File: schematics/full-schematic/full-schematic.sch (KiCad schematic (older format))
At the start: 24 parts, among them SW1 SW_SPST, SW2 SW_Push_Dual, SW3 SW_Push_Dual, SW4 SW_SPDT, U1 L7805, U2 74LS04, U5 LP3470, X1 CXO_DIP8

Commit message: Schematics
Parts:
- added TP2, TP3: TestPoint_Probe, TestPoint:TestPoint_Pad_D1.5mm, symbol Connector:TestPoint_Probe
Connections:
- net -RST-: now also TP2.1
- net SYS_CLK: now also TP3.1
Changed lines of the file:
@@
 EESchema Schematic File Version 4
-LIBS:full-schematic-cache
-EELAYER 29 0
+EELAYER 30 0
 EELAYER END
 $Descr A4 11693 8268
 encoding utf-8
-Sheet 1 3
+Sheet 1 4
 Title ""
 Date ""
@@
 	3400 5600 4050 5600
 Wire Wire Line
-	4550 6100 5000 6100
-Text Label 5000 6100 2    50   ~ 0
-SYS_CLK
+	4550 6100 4800 6100
 $Comp
 L power:VDD #PWR0101
@@
 	1    0    0    -1
 $EndComp
-$Comp
-L power:GND #PWR010
-U 1 1 5D4C31C1
-P 3900 4150
-F 0 "#PWR010" H 3900 3900 50  0001 C CNN
-F 1 "GND" H 3905 3977 50  0000 C CNN
-F 2 "" H 3900 4150 50  0001 C CNN
-F 3 "" H 3900 4150 50  0001 C CNN
-	1    3900 4150
-	1    0    0    -1
-$EndComp
-Wire Wire Line
-	3750 3700 3900 3700
-Connection ~ 3900 3700
-Wire Wire Line
-	3900 3850 3900 3700
 Wire Wire Line
 	3350 3700 3450 3700
 Wire Wire Line
 	3350 3550 3350 3700
-$Comp
-L Device:C C6
-U 1 1 5D4B9F93
-P 3900 4000
-F 0 "C6" H 4015 4046 50  0000 L CNN
-F 1 "0.1u" H 4015 3955 50  0000 L CNN
-F 2 "Capacitor_SMD:C_0603_1608Metric_Pad1.05x0.95mm_HandSolder" H 3938 3850 50  0001 C CNN
-F 3 "~" H 3900 4000 50  0001 C CNN
-	1    3900 4000
-	1    0    0    -1
-$EndComp
 $Comp
 L Device:R R5
@@
 $EndSheet
 Wire Wire Line
-	4050 3700 3900 3700
-Text Label 5650 4100 2    50   ~ 0
--RST-
-Wire Wire Line
-	5350 4100 5650 4100
-Wire Wire Line
-	4700 3700 5650 3700
-Connection ~ 4700 3700
-Wire Wire Line
-	4700 4100 4750 4100
-Wire Wire Line
-	4700 3700 4700 4100
+	5350 4100 5450 4100
+$Comp
+L z80-project:LP3470 U5
+U 1 1 5DDDF23A
+P 2100 3350
+F 0 "U5" H 1800 3650 50  0000 L CNN
+F 1 "LP3470" H 2200 3650 50  0000 L CNN
+F 2 "Package_TO_SOT_SMD:SOT-23-5_HandSoldering" H 3100 3000 50  0001 C CNN
+F 3 "https://www.promelec.ru/pdf/LP3470.pdf" H 3100 3000 50  0001 C CNN
+	1    2100 3350
+	1    0    0    -1
+$EndComp
+$Comp
+L power:GND #PWR017
+U 1 1 5DE0F4DA
+P 2100 4400
+F 0 "#PWR017" H 2100 4150 50  0001 C CNN
+F 1 "GND" H 2105 4227 50  0000 C CNN
+F 2 "" H 2100 4400 50  0001 C CNN
+F 3 "" H 2100 4400 50  0001 C CNN
+	1    2100 4400
+	1    0    0    -1
+$EndComp
+$Comp
+L power:+5V #PWR06
+U 1 1 5DE116D4
+P 2100 2850
+F 0 "#PWR06" H 2100 2700 50  0001 C CNN
+F 1 "+5V" H 2115 3023 50  0000 C CNN
+F 2 "" H 2100 2850 50  0001 C CNN
+F 3 "" H 2100 2850 50  0001 C CNN
+	1    2100 2850
+	1    0    0    -1
+$EndComp
+Wire Wire Line
+	1550 3200 1600 3200
+$Comp
+L Device:C C9
+U 1 1 5DE1D4C5
+P 1450 3700
+F 0 "C9" H 1565 3746 50  0000 L CNN
+F 1 "0.1u" H 1565 3655 50  0000 L CNN
+F 2 "Capacitor_SMD:C_0603_1608Metric_Pad1.05x0.95mm_HandSolder" H 1488 3550 50  0001 C CNN
+F 3 "~" H 1450 3700 50  0001 C CNN
+	1    1450 3700
+	1    0    0    -1
+$EndComp
+$Comp
+L power:GND #PWR05
+U 1 1 5DE1D99B
+P 1450 3850
+F 0 "#PWR05" H 1450 3600 50  0001 C CNN
+F 1 "GND" H 1455 3677 50  0000 C CNN
+F 2 "" H 1450 3850 50  0001 C CNN
+F 3 "" H 1450 3850 50  0001 C CNN
+	1    1450 3850
+	1    0    0    -1
+$EndComp
+Wire Wire Line
+	2100 2900 2100 3000
+Wire Wire Line
+	1550 2900 1550 3200
+Connection ~ 2100 2900
+Wire Wire Line
+	2100 2900 1550 2900
+Wire Wire Line
+	2100 2850 2100 2900
+Wire Wire Line
+	1450 3550 1450 3500
+Wire Wire Line
+	1450 3500 1600 3500
+$Sheet
+S 9500 1000 1500 500
+U 5DEAD379
+F0 "IC-Power" 50
+F1 "IC-Power.sch" 50
+$EndSheet
+Wire Wire Line
+	2650 3950 2700 3950
+Wire Wire Line
+	2700 4150 2650 4150
+Wire Wire Line
+	2100 3700 2100 3950
+Wire Wire Line
+	2250 3950 2100 3950
+Connection ~ 2100 3950
+Wire Wire Line
+	2100 3950 2100 4150
+Wire Wire Line
+	2250 4150 2100 4150
+Connection ~ 2100 4150
+Wire Wire Line
+	2100 4150 2100 4400
+$Comp
+L Device:D_Schottky D3
+U 1 1 5E366A87
+P 2900 3350
+F 0 "D3" H 2900 3250 50  0000 C CNN
+F 1 "D_Schottky" H 2900 3450 50  0000 C CNN
+F 2 "Diode_SMD:D_0603_1608Metric_Pad1.05x0.95mm_HandSolder" H 2900 3350 50  0001 C CNN
+F 3 "~" H 2900 3350 50  0001 C CNN
+	1    2900 3350
+	1    0    0    -1
+$EndComp
+Wire Wire Line
+	2750 3350 2600 3350
+Wire Wire Line
+	2700 3950 2700 4050
+Connection ~ 2700 4050
+Wire Wire Line
+	2700 4050 2700 4150
+Wire Wire Line
+	3050 3350 3200 3350
+Wire Wire Line
+	3200 3350 3200 3700
+Connection ~ 3200 3700
+Wire Wire Line
+	3200 3700 3200 4050
+Wire Wire Line
+	3200 3700 3350 3700
+Connection ~ 3350 3700
+Wire Wire Line
+	2700 4050 3200 4050
+Wire Wire Line
+	4650 3700 4700 3700
+$Comp
+L 74xx:74LS04 U2
+U 1 1 5D5B39DE
+P 4350 3700
+F 0 "U2" H 4350 4017 50  0000 C CNN
+F 1 "74LS04" H 4350 3926 50  0000 C CNN
+F 2 "Package_SO:SOIC-14_3.9x8.7mm_P1.27mm" H 4350 3700 50  0001 C CNN
+F 3 "http://www.ti.com/lit/gpn/sn74LS04" H 4350 3700 50  0001 C CNN
+	1    4350 3700
+	1    0    0    -1
+$EndComp
 $Comp
 L 74xx:74LS04 U2
@@
 	1    0    0    -1
 $EndComp
-Text Label 5650 3700 2    50   ~ 0
+Wire Wire Line
+	4700 3700 4700 4100
+Wire Wire Line
+	4700 4100 4750 4100
+Connection ~ 4700 3700
+Wire Wire Line
+	4700 3700 5650 3700
+Wire Wire Line
+	4050 3700 3900 3700
+$Comp
+L Device:C C6
+U 1 1 5D4B9F93
+P 3900 4000
+F 0 "C6" H 4015 4046 50  0000 L CNN
+F 1 "0.1u" H 4015 3955 50  0000 L CNN
+F 2 "Capacitor_SMD:C_0603_1608Metric_Pad1.05x0.95mm_HandSolder" H 3938 3850 50  0001 C CNN
+F 3 "~" H 3900 4000 50  0001 C CNN
+	1    3900 4000
+	1    0    0    -1
+$EndComp
+Wire Wire Line
+	3900 3850 3900 3700
+Connection ~ 3900 3700
+Wire Wire Line
+	3750 3700 3900 3700
+$Comp
+L power:GND #PWR010
+U 1 1 5D4C31C1
+P 3900 4150
+F 0 "#PWR010" H 3900 3900 50  0001 C CNN
+F 1 "GND" H 3905 3977 50  0000 C CNN
+F 2 "" H 3900 4150 50  0001 C CNN
+F 3 "" H 3900 4150 50  0001 C CNN
+	1    3900 4150
+	1    0    0    -1
+$EndComp
+Text GLabel 5650 3700 2    50   Input ~ 0
 RST
-$Comp
-L 74xx:74LS04 U2
-U 1 1 5D5B39DE
-P 4350 3700
-F 0 "U2" H 4350 4017 50  0000 C CNN
-F 1 "74LS04" H 4350 3926 50  0000 C CNN
-F 2 "Package_SO:SOIC-14_3.9x8.7mm_P1.27mm" H 4350 3700 50  0001 C CNN
-F 3 "http://www.ti.com/lit/gpn/sn74LS04" H 4350 3700 50  0001 C CNN
-	1    4350 3700
-	1    0    0    -1
-$EndComp
-Wire Wire Line
-	4650 3700 4700 3700
-$Comp
-L z80-project:LP3470 U5
-U 1 1 5DDDF23A
-P 2100 3350
-F 0 "U5" H 1800 3650 50  0000 L CNN
-F 1 "LP3470" H 2200 3650 50  0000 L CNN
-F 2 "Package_TO_SOT_SMD:SOT-23-5_HandSoldering" H 3100 3000 50  0001 C CNN
-F 3 "https://www.promelec.ru/pdf/LP3470.pdf" H 3100 3000 50  0001 C CNN
-	1    2100 3350
-	1    0    0    -1
-$EndComp
-$Comp
-L power:GND #PWR017
-U 1 1 5DE0F4DA
-P 2100 4400
-F 0 "#PWR017" H 2100 4150 50  0001 C CNN
-F 1 "GND" H 2105 4227 50  0000 C CNN
-F 2 "" H 2100 4400 50  0001 C CNN
-F 3 "" H 2100 4400 50  0001 C CNN
-	1    2100 4400
-	1    0    0    -1
-$EndComp
-$Comp
-L power:+5V #PWR06
-U 1 1 5DE116D4
-P 2100 2850
-F 0 "#PWR06" H 2100 2700 50  0001 C CNN
-F 1 "+5V" H 2115 3023 50  0000 C CNN
-F 2 "" H 2100 2850 50  0001 C CNN
-F 3 "" H 2100 2850 50  0001 C CNN
-	1    2100 2850
-	1    0    0    -1
-$EndComp
-Wire Wire Line
-	1550 3200 1600 3200
-$Comp
-L Device:C C9
-U 1 1 5DE1D4C5
-P 1450 3700
-F 0 "C9" H 1565 3746 50  0000 L CNN
-F 1 "0.1u" H 1565 3655 50  0000 L CNN
-F 2 "Capacitor_SMD:C_0603_1608Metric_Pad1.05x0.95mm_HandSolder" H 1488 3550 50  0001 C CNN
-F 3 "~" H 1450 3700 50  0001 C CNN
-	1    1450 3700
-	1    0    0    -1
-$EndComp
-$Comp
-L power:GND #PWR05
-U 1 1 5DE1D99B
-P 1450 3850
-F 0 "#PWR05" H 1450 3600 50  0001 C CNN
-F 1 "GND" H 1455 3677 50  0000 C CNN
-F 2 "" H 1450 3850 50  0001 C CNN
-F 3 "" H 1450 3850 50  0001 C CNN
-	1    1450 3850
-	1    0    0    -1
-$EndComp
-Wire Wire Line
-	2100 2900 2100 3000
-Wire Wire Line
-	1550 2900 1550 3200
-Connection ~ 2100 2900
-Wire Wire Line
-	2100 2900 1550 2900
-Wire Wire Line
-	2100 2850 2100 2900
-Wire Wire Line
-	1450 3550 1450 3500
-Wire Wire Line
-	1450 3500 1600 3500
+Text GLabel 5650 4100 2    50   Input ~ 0
+-RST-
+Text GLabel 5000 6100 2    50   Input ~ 0
+SYS_CLK
+$Comp
+L Connector:TestPoint_Probe TP2
+U 1 1 5DFF4C3F
+P 5450 4350
+F 0 "TP2" V 5458 4503 50  0000 L CNN
+F 1 "TestPoint_Probe" V 5549 4503 50  0000 L CNN
+F 2 "TestPoint:TestPoint_Pad_D1.5mm" H 5650 4350 50  0001 C CNN
+F 3 "~" H 5650 4350 50  0001 C CNN
+	1    5450 4350
+	0    1    1    0
+$EndComp
+Wire Wire Line
+	5450 4350 5450 4100
+Connection ~ 5450 4100
+Wire Wire Line
+	5450 4100 5650 4100
+$Comp
+L Connector:TestPoint_Probe TP3
+U 1 1 5DFF800C
+P 4800 5850
+F 0 "TP3" H 4953 5951 50  0000 L CNN
+F 1 "TestPoint_Probe" H 4953 5860 50  0000 L CNN
+F 2 "TestPoint:TestPoint_Pad_D1.5mm" H 5000 5850 50  0001 C CNN
+F 3 "~" H 5000 5850 50  0001 C CNN
+	1    4800 5850
+	1    0    0    -1
+$EndComp
+Wire Wire Line
+	4800 5850 4800 6100
+Connection ~ 4800 6100
+Wire Wire Line
+	4800 6100 5000 6100
 $Sheet
-S 9500 1000 1500 500
-U 5DEAD379
-F0 "IC-Power" 50
-F1 "IC-Power.sch" 50
+S 9500 2500 1500 500
+U 5DFFC633
+F0 "Memory" 50
+F1 "Memory.sch" 50
 $EndSheet
-Wire Wire Line
-	2650 3950 2700 3950
-Wire Wire Line
-	2700 4150 2650 4150
-Wire Wire Line
-	2100 3700 2100 3950
-Wire Wire Line
-	2250 3950 2100 3950
-Connection ~ 2100 3950
-Wire Wire Line
-	2100 3950 2100 4150
-Wire Wire Line
-	2250 4150 2100 4150
-Connection ~ 2100 4150
-Wire Wire Line
-	2100 4150 2100 4400
-$Comp
-L Device:D_Schottky D3
-U 1 1 5E366A87
-P 2900 3350
-F 0 "D3" H 2900 3250 50  0000 C CNN
-F 1 "D_Schottky" H 2900 3450 50  0000 C CNN
-F 2 "Diode_SMD:D_0603_1608Metric_Pad1.05x0.95mm_HandSolder" H 2900 3350 50  0001 C CNN
-F 3 "~" H 2900 3350 50  0001 C CNN
-	1    2900 3350
-	1    0    0    -1
-$EndComp
-Wire Wire Line
-	2750 3350 2600 3350
-Wire Wire Line
-	2700 3950 2700 4050
-Connection ~ 2700 4050
-Wire Wire Line
-	2700 4050 2700 4150
-Wire Wire Line
-	3050 3350 3200 3350
-Wire Wire Line
-	3200 3350 3200 3700
-Connection ~ 3200 3700
-Wire Wire Line
-	3200 3700 3200 4050
-Wire Wire Line
-	3200 3700 3350 3700
-Connection ~ 3350 3700
-Wire Wire Line
-	2700 4050 3200 4050
 $EndSCHEMATC

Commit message: Schematics
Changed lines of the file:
@@
 EESchema Schematic File Version 4
+LIBS:full-schematic-cache
 EELAYER 30 0
 EELAYER END
@@
 	5350 4100 5450 4100
 $Comp
-L z80-project:LP3470 U5
-U 1 1 5DDDF23A
-P 2100 3350
-F 0 "U5" H 1800 3650 50  0000 L CNN
-F 1 "LP3470" H 2200 3650 50  0000 L CNN
-F 2 "Package_TO_SOT_SMD:SOT-23-5_HandSoldering" H 3100 3000 50  0001 C CNN
-F 3 "https://www.promelec.ru/pdf/LP3470.pdf" H 3100 3000 50  0001 C CNN
-	1    2100 3350
-	1    0    0    -1
-$EndComp
-$Comp
 L power:GND #PWR017
 U 1 1 5DE0F4DA
@@
 F1 "Memory.sch" 50
 $EndSheet
+$Comp
+L z80-project:LP3470 U5
+U 1 1 5DFC8620
+P 2100 3350
+F 0 "U5" H 2300 3650 50  0000 L CNN
+F 1 "LP3470" H 2200 3050 50  0000 L CNN
+F 2 "Package_TO_SOT_SMD:SOT-23-5_HandSoldering" H 3100 3000 50  0001 C CNN
+F 3 "https://www.promelec.ru/pdf/LP3470.pdf" H 3100 3000 50  0001 C CNN
+	1    2100 3350
+	1    0    0    -1
+$EndComp
 $EndSCHEMATC

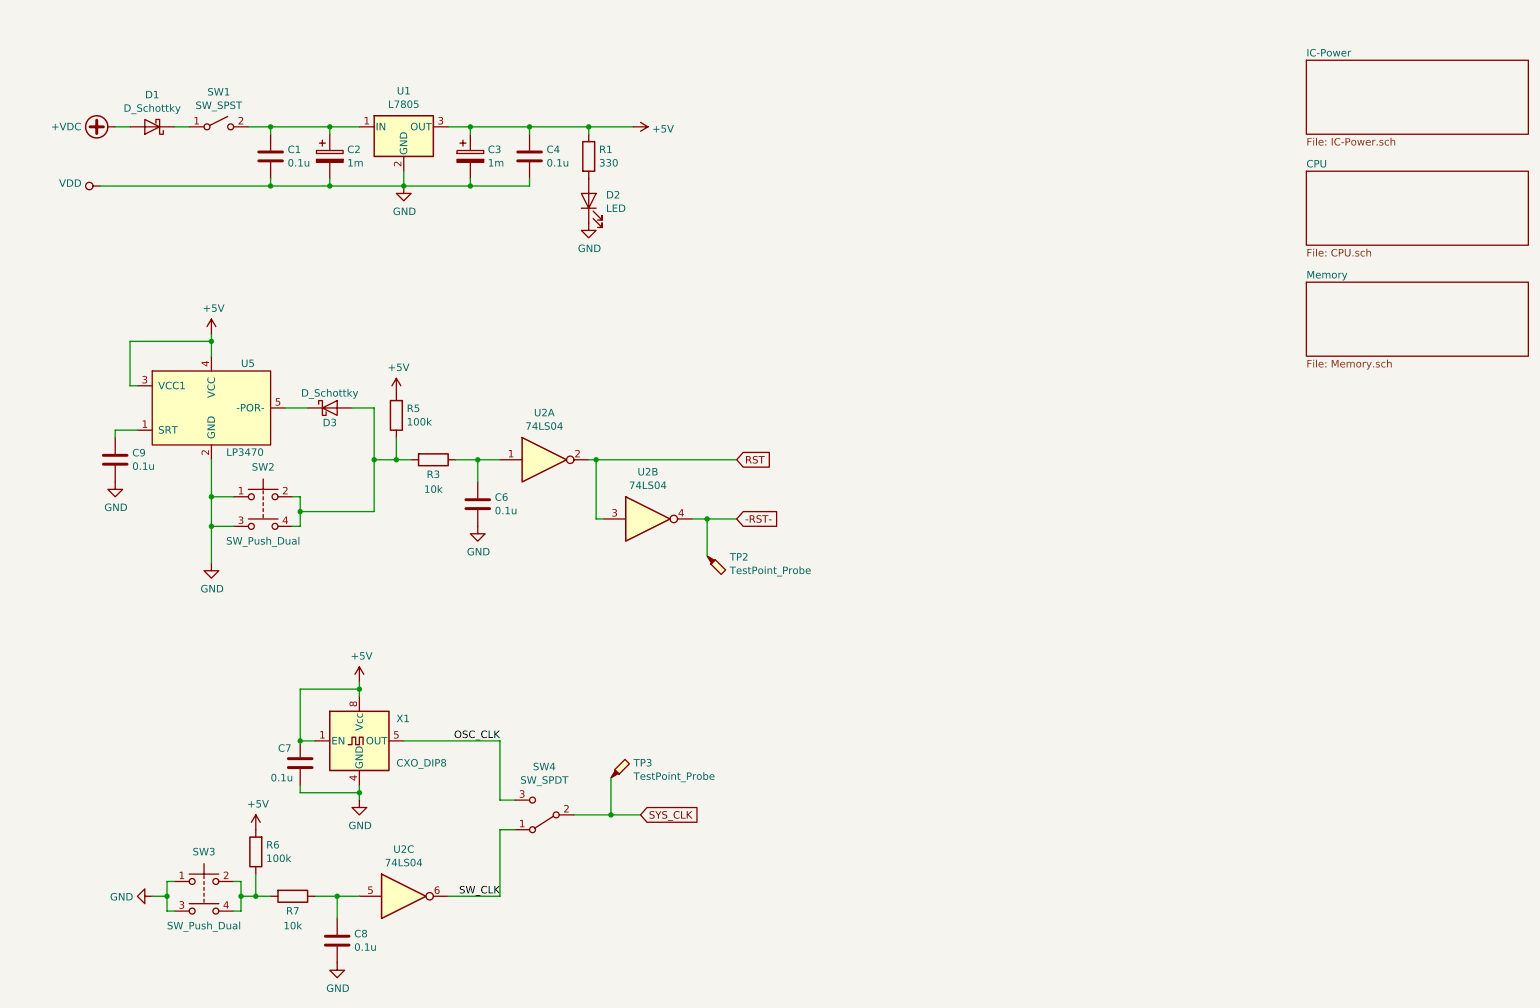
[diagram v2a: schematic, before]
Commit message: Schematic updates
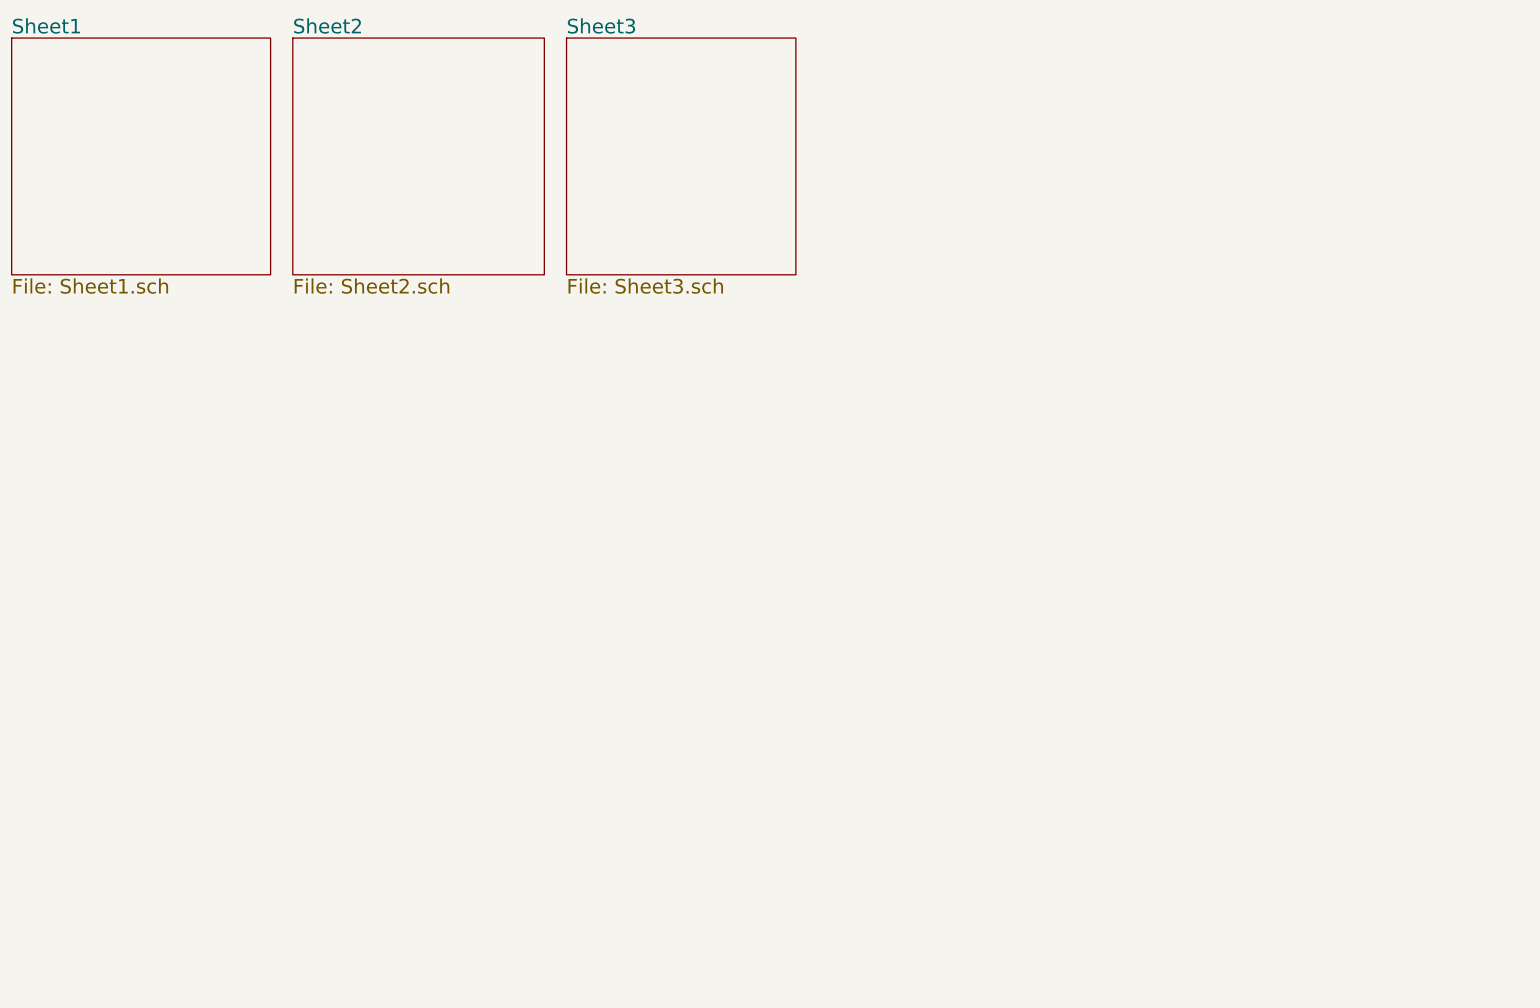
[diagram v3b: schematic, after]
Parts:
- removed C1, C4, C6, C7, C8, C9: 0.1u, Capacitor_SMD:C_0603_1608Metric_Pad1.05x0.95mm_HandSolder, symbol Device:C
- removed C2, C3: 1m, Capacitor_SMD:C_0603_1608Metric_Pad1.05x0.95mm_HandSolder, symbol Device:CP
- removed D1, D3: D_Schottky, Diode_SMD:D_0603_1608Metric_Pad1.05x0.95mm_HandSolder, symbol Device:D_Schottky
- removed D2: LED, LED_SMD:LED_0603_1608Metric_Pad1.05x0.95mm_HandSolder, symbol Device:LED
- removed R1: 330, Resistor_SMD:R_0603_1608Metric_Pad1.05x0.95mm_HandSolder, symbol Device:R
- removed R3, R7: 10k, Resistor_SMD:R_0603_1608Metric_Pad1.05x0.95mm_HandSolder, symbol Device:R
- removed R5, R6: 100k, Resistor_SMD:R_0603_1608Metric_Pad1.05x0.95mm_HandSolder, symbol Device:R
- removed SW1: SW_SPST, symbol Switch:SW_SPST
- removed SW2, SW3: SW_Push_Dual, Button_Switch_SMD:SW_MEC_5GSH9, symbol Switch:SW_Push_Dual
- removed SW4: SW_SPDT, symbol Switch:SW_SPDT
- removed TP2, TP3: TestPoint_Probe, TestPoint:TestPoint_Pad_D1.5mm, symbol Connector:TestPoint_Probe
- removed U1: L7805, Package_TO_SOT_SMD:TO-263-2, symbol Regulator_Linear:L7805
- removed U2: 74LS04, Package_SO:SOIC-14_3.9x8.7mm_P1.27mm, symbol 74xx:74LS04
- removed U5: LP3470, Package_TO_SOT_SMD:SOT-23-5_HandSoldering, symbol z80-project:LP3470
- removed X1: CXO_DIP8, Oscillator:Oscillator_DIP-8, symbol Oscillator:CXO_DIP8
